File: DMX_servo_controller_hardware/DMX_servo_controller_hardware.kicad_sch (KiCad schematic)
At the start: 69 parts, among them J1 Power connector, J10 Conn_01x03, J11 Conn_01x03, J12 Conn_01x03, J15 To_XLR3, J3 Display, J4 Rotary encoder, J5 Conn_01x03, J6 Conn_01x03, J7 Conn_01x03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

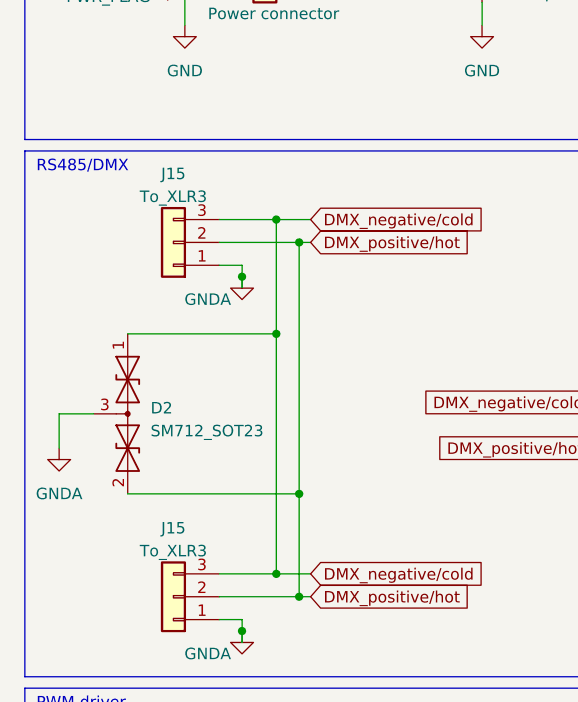
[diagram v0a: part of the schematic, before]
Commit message: Assigns footprint for test points
We might want to have all test points going to one connector (01x06 pin
header) to make the layout easier in the future.
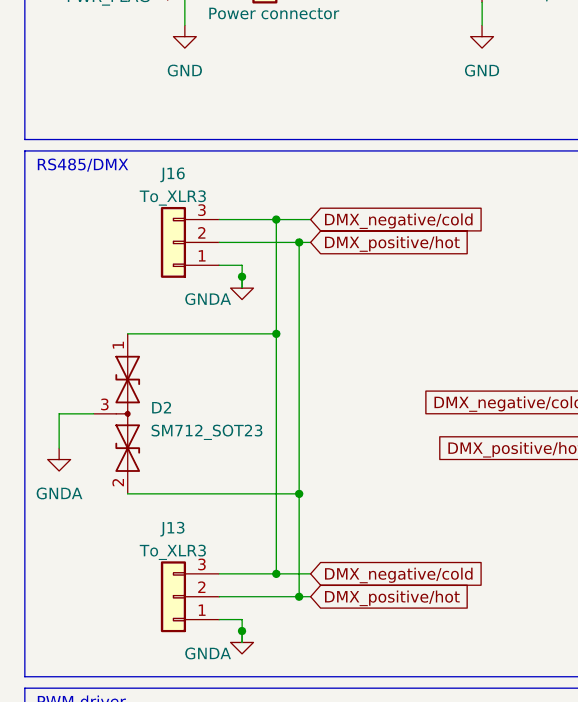
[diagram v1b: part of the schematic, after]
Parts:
- TP1, TP2, TP3, TP4, TP5, TP6, TP7, TP8: footprint (none) -> Connector_PinHeader_2.54mm:PinHeader_1x01_P2.54mm_Vertical
- renumbered J15 to J13, J15 to J16
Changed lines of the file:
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@@
       (effects (font (size 1.27 1.27)) (justify left))
     )
-    (property "Footprint" "" (at 124.46 149.86 0)
+    (property "Footprint" "Connector_PinHeader_2.54mm:PinHeader_1x01_P2.54mm_Vertical" (at 124.46 149.86 0)
       (effects (font (size 1.27 1.27)) hide)
     )
@@
       (effects (font (size 1.27 1.27)) (justify left))
     )
-    (property "Footprint" "" (at 124.46 157.48 0)
+    (property "Footprint" "Connector_PinHeader_2.54mm:PinHeader_1x01_P2.54mm_Vertical" (at 124.46 157.48 0)
       (effects (font (size 1.27 1.27)) hide)
     )
@@
       (effects (font (size 1.27 1.27)) (justify left))
     )
-    (property "Footprint" "" (at 124.46 160.02 0)
+    (property "Footprint" "Connector_PinHeader_2.54mm:PinHeader_1x01_P2.54mm_Vertical" (at 124.46 160.02 0)
       (effects (font (size 1.27 1.27)) hide)
     )
@@
       (effects (font (size 1.27 1.27)) (justify left))
     )
-    (property "Footprint" "" (at 124.46 152.4 0)
+    (property "Footprint" "Connector_PinHeader_2.54mm:PinHeader_1x01_P2.54mm_Vertical" (at 124.46 152.4 0)
       (effects (font (size 1.27 1.27)) hide)
     )
@@
       (effects (font (size 1.27 1.27)) (justify left))
     )
-    (property "Footprint" "" (at 124.46 162.56 0)
+    (property "Footprint" "Connector_PinHeader_2.54mm:PinHeader_1x01_P2.54mm_Vertical" (at 124.46 162.56 0)
       (effects (font (size 1.27 1.27)) hide)
     )
@@
       (effects (font (size 1.27 1.27)) (justify left))
     )
-    (property "Footprint" "" (at 124.46 154.94 0)
+    (property "Footprint" "Connector_PinHeader_2.54mm:PinHeader_1x01_P2.54mm_Vertical" (at 124.46 154.94 0)
       (effects (font (size 1.27 1.27)) hide)
     )
@@
   (symbol (lib_id "Connector_Generic:Conn_01x03") (at 29.21 97.79 180) (unit 1)
     (in_bom yes) (on_board yes) (dnp no) (fields_autoplaced)
-    (property "Reference" "J15" (at 29.21 90.17 0)
+    (property "Reference" "J13" (at 29.21 90.17 0)
       (effects (font (size 1.27 1.27)))
     )
@@
       (effects (font (size 1.27 1.27)) (justify left))
     )
-    (property "Footprint" "" (at 124.46 167.64 0)
+    (property "Footprint" "Connector_PinHeader_2.54mm:PinHeader_1x01_P2.54mm_Vertical" (at 124.46 167.64 0)
       (effects (font (size 1.27 1.27)) hide)
     )
@@
   (symbol (lib_id "Connector_Generic:Conn_01x03") (at 29.21 58.42 180) (unit 1)
     (in_bom yes) (on_board yes) (dnp no) (fields_autoplaced)
-    (property "Reference" "J15" (at 29.21 50.8 0)
+    (property "Reference" "J16" (at 29.21 50.8 0)
       (effects (font (size 1.27 1.27)))
     )
@@
       (effects (font (size 1.27 1.27)) (justify left))
     )
-    (property "Footprint" "" (at 124.46 165.1 0)
-      (effects (font (size 1.27 1.27)) hide)
-    )
+    (property "Footprint" "Connector_PinHeader_2.54mm:PinHeader_1x01_P2.54mm_Vertical" (at 124.46 165.1 0)
+      (effects (font (size 1.27 1.27)) hide)
+    )

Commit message: Reorder JST conectors and PCA9685 outputs for completion (OCD) / added DNP in 4out8 outputs / removed unnecessary resistor for upper 8 outputs of PCA9685 testpoints
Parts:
- removed R21, R22, R23, R24, R25, R26, R27, R28: 220Ω, Resistor_SMD:R_0815_2038Metric_Pad1.20x4.05mm_HandSolder, symbol Device:R_US
- J10, J11, J12, J9, R17, R18, R19, R20: now not fitted
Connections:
- net OUT1: now also J6.2 (Pin_2); no longer J7.2 (Pin_2)
- net OUT2: now also J7.2 (Pin_2); no longer J9.2 (Pin_2)
- net OUT3: now also J8.2 (Pin_2); no longer J11.2 (Pin_2)
- net OUT4: now also J9.2 (Pin_2); no longer J6.2 (Pin_2)
- net OUT5: now also J10.2 (Pin_2); no longer J8.2 (Pin_2)
- net OUT6: now also J11.2 (Pin_2); no longer J10.2 (Pin_2)
- net at U1.21 (LED14): now also TP7.1
- net at U1.20 (LED13): now also TP6.1
- net at U1.22 (LED15): now also TP8.1
- net at TP1.1: now also U1.15 (LED8)
- net at U1.16 (LED9): now also TP2.1
- net at U1.17 (LED10): now also TP3.1
- net at U1.18 (LED11): now also TP4.1
- net at U1.19 (LED12): now also TP5.1
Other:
- moved on the sheet: J6, J7, J8, R6, TP1, TP2, TP3, TP4, TP5, TP6, TP7, TP8

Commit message: Adds footprint for reset pushbutton
The footprint almost matches (and is definitely within tolerances) for
the technical drawing and measurements taken from the pushbuttons to be
used.
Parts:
- SW1: footprint (none) -> Button_Switch_SMD:SW_SPST_TL3342
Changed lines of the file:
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@@
       (effects (font (size 1.27 1.27)))
     )
-    (property "Footprint" "" (at 209.55 88.9 0)
+    (property "Footprint" "Button_Switch_SMD:SW_SPST_TL3342" (at 209.55 88.9 0)
       (effects (font (size 1.27 1.27)) hide)
     )

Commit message: Adds 6N137-X007T footprint and assigns it in schematics
The X007 variant of 6N137 uses an SMD gullwing package. The footprint
was created following the technical drawing in vishay's datasheet[1].

[1]: https://www.vishay.com/docs/84732/6n137.pdf
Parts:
- U3: footprint Package_DIP:DIP-8_W7.62mm -> DMX_servo_controller_hardware:6N137-X007T
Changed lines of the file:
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@@
       (effects (font (size 1.27 1.27)))
     )
-    (property "Footprint" "Package_DIP:DIP-8_W7.62mm" (at 151.13 81.28 0)
+    (property "Footprint" "DMX_servo_controller_hardware:6N137-X007T" (at 151.13 81.28 0)
       (effects (font (size 1.27 1.27)) hide)
     )

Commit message: Uses screw terminals for servo output connectors
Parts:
- J10, J11, J12, J5, J6, J7, J8, J9: footprint Connector_JST:JST_XH_B3B-XH-AM_1x03_P2.50mm_Vertical -> TerminalBlock:TerminalBlock_bornier-3_P5.08mm
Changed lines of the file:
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@@
       (effects (font (size 1.27 1.27)) (justify left))
     )
-    (property "Footprint" "Connector_JST:JST_XH_B3B-XH-AM_1x03_P2.50mm_Vertical" (at 182.88 123.19 0)
+    (property "Footprint" "TerminalBlock:TerminalBlock_bornier-3_P5.08mm" (at 182.88 123.19 0)
       (effects (font (size 1.27 1.27)) hide)
     )
@@
       (effects (font (size 1.27 1.27)) (justify left))
     )
-    (property "Footprint" "Connector_JST:JST_XH_B3B-XH-AM_1x03_P2.50mm_Vertical" (at 210.82 151.13 0)
+    (property "Footprint" "TerminalBlock:TerminalBlock_bornier-3_P5.08mm" (at 210.82 151.13 0)
       (effects (font (size 1.27 1.27)) hide)
     )
@@
       (effects (font (size 1.27 1.27)) (justify left))
     )
-    (property "Footprint" "Connector_JST:JST_XH_B3B-XH-AM_1x03_P2.50mm_Vertical" (at 210.82 123.19 0)
+    (property "Footprint" "TerminalBlock:TerminalBlock_bornier-3_P5.08mm" (at 210.82 123.19 0)
       (effects (font (size 1.27 1.27)) hide)
     )
@@
       (effects (font (size 1.27 1.27)) (justify left))
     )
-    (property "Footprint" "Connector_JST:JST_XH_B3B-XH-AM_1x03_P2.50mm_Vertical" (at 182.88 151.13 0)
+    (property "Footprint" "TerminalBlock:TerminalBlock_bornier-3_P5.08mm" (at 182.88 151.13 0)
       (effects (font (size 1.27 1.27)) hide)
     )
@@
       (effects (font (size 1.27 1.27)) (justify left))
     )
-    (property "Footprint" "Connector_JST:JST_XH_B3B-XH-AM_1x03_P2.50mm_Vertical" (at 238.76 151.13 0)
+    (property "Footprint" "TerminalBlock:TerminalBlock_bornier-3_P5.08mm" (at 238.76 151.13 0)
       (effects (font (size 1.27 1.27)) hide)
     )
@@
       (effects (font (size 1.27 1.27)) (justify left))
     )
-    (property "Footprint" "Connector_JST:JST_XH_B3B-XH-AM_1x03_P2.50mm_Vertical" (at 266.7 123.19 0)
+    (property "Footprint" "TerminalBlock:TerminalBlock_bornier-3_P5.08mm" (at 266.7 123.19 0)
       (effects (font (size 1.27 1.27)) hide)
     )
@@
       (effects (font (size 1.27 1.27)) (justify left))
     )
-    (property "Footprint" "Connector_JST:JST_XH_B3B-XH-AM_1x03_P2.50mm_Vertical" (at 238.76 123.19 0)
+    (property "Footprint" "TerminalBlock:TerminalBlock_bornier-3_P5.08mm" (at 238.76 123.19 0)
       (effects (font (size 1.27 1.27)) hide)
     )
@@
       (effects (font (size 1.27 1.27)) (justify left))
     )
-    (property "Footprint" "Connector_JST:JST_XH_B3B-XH-AM_1x03_P2.50mm_Vertical" (at 266.7 149.86 0)
-      (effects (font (size 1.27 1.27)) hide)
-    )
+    (property "Footprint" "TerminalBlock:TerminalBlock_bornier-3_P5.08mm" (at 266.7 149.86 0)
+      (effects (font (size 1.27 1.27)) hide)
+    )

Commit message: Uses DIP-8 footprint for SN65HVD12
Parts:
- U2: footprint Package_SO:SOIC-8_3.9x4.9mm_P1.27mm -> Package_DIP:DIP-8_W7.62mm
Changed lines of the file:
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@@
       (effects (font (size 1.27 1.27)) (justify right))
     )
-    (property "Footprint" "Package_SO:SOIC-8_3.9x4.9mm_P1.27mm" (at 110.49 55.88 0)
+    (property "Footprint" "Package_DIP:DIP-8_W7.62mm" (at 110.49 55.88 0)
       (effects (font (size 1.27 1.27)) hide)
     )

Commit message: Switches symbol and footprint for diode on VUSB
We're using the C211752[1] from yangjie, but since there's no schematic
symbol for it, I replaced it with the MRA4003T3G since it has the same
functionality and footprint and changed the value to reflect the correct
part number.

[1]: https://datasheet.lcsc.com/lcsc/1912111437_Yangzhou-Yangjie-Elec-Tech-M7_C211752.pdf
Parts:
- removed D1: 1N4001, Diode_THT:D_DO-41_SOD81_P10.16mm_Horizontal, symbol Diode:1N4001
- added D3: C211752 M7, Diode_SMD:D_SMA, symbol Diode:MRA4003T3G
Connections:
- net +5V: now also D3.2 (A)
- net at U4.40 (VBUS): now also D3.1 (K)
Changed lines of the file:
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@@
-    )
-  )
-  (symbol (lib_id "Diode:1N4001") (at 259.08 27.94 90) (unit 1)
-    (in_bom yes) (on_board yes) (dnp no) (fields_autoplaced)
-    (property "Reference" "D1" (at 261.62 27.305 90)
-      (effects (font (size 1.27 1.27)) (justify right))
-    )
-    (property "Value" "1N4001" (at 261.62 29.845 90)
-      (effects (font (size 1.27 1.27)) (justify right))
-    )
-    (property "Footprint" "Diode_THT:D_DO-41_SOD81_P10.16mm_Horizontal" (at 259.08 27.94 0)
-      (effects (font (size 1.27 1.27)) hide)
-    )
-    (property "Datasheet" "http://www.vishay.com/docs/88503/1n4001.pdf" (at 259.08 27.94 0)
-      (effects (font (size 1.27 1.27)) hide)
-    )
-    (pin "1")
-    (pin "2")
-    (instances
-      (project "DMX_servo_controller_hardware"
-        (path "/cd90393c-7fb4-4867-84b8-7df1a2bf6613"
-          (reference "D1") (unit 1)
-        )
-      )
     )
   )
@@
         )
       )
+    )
+  )
+  (symbol (lib_id "Diode:MRA4003T3G") (at 259.08 27.94 90) (unit 1)
+    (in_bom yes) (on_board yes) (dnp no) (fields_autoplaced)
+    (property "Reference" "D3" (at 261.62 27.305 90)
+      (effects (font (size 1.27 1.27)) (justify right))
+    )
+    (property "Value" "C211752 M7" (at 261.62 29.845 90)
+      (effects (font (size 1.27 1.27)) (justify right))
+    )
+    (property "Footprint" "Diode_SMD:D_SMA" (at 263.525 27.94 0)
+      (effects (font (size 1.27 1.27)) hide)
+    )
+    (property "Datasheet" "https://datasheet.lcsc.com/lcsc/1912111437_Yangzhou-Yangjie-Elec-Tech-M7_C211752.pdf" (at 259.08 27.94 0)
+      (effects (font (size 1.27 1.27)) hide)
+    )
+    (pin "1")
+    (pin "2")
+    (instances
+      (project "DMX_servo_controller_hardware"
+        (path "/cd90393c-7fb4-4867-84b8-7df1a2bf6613"
+          (reference "D3") (unit 1)
+        )
+      )

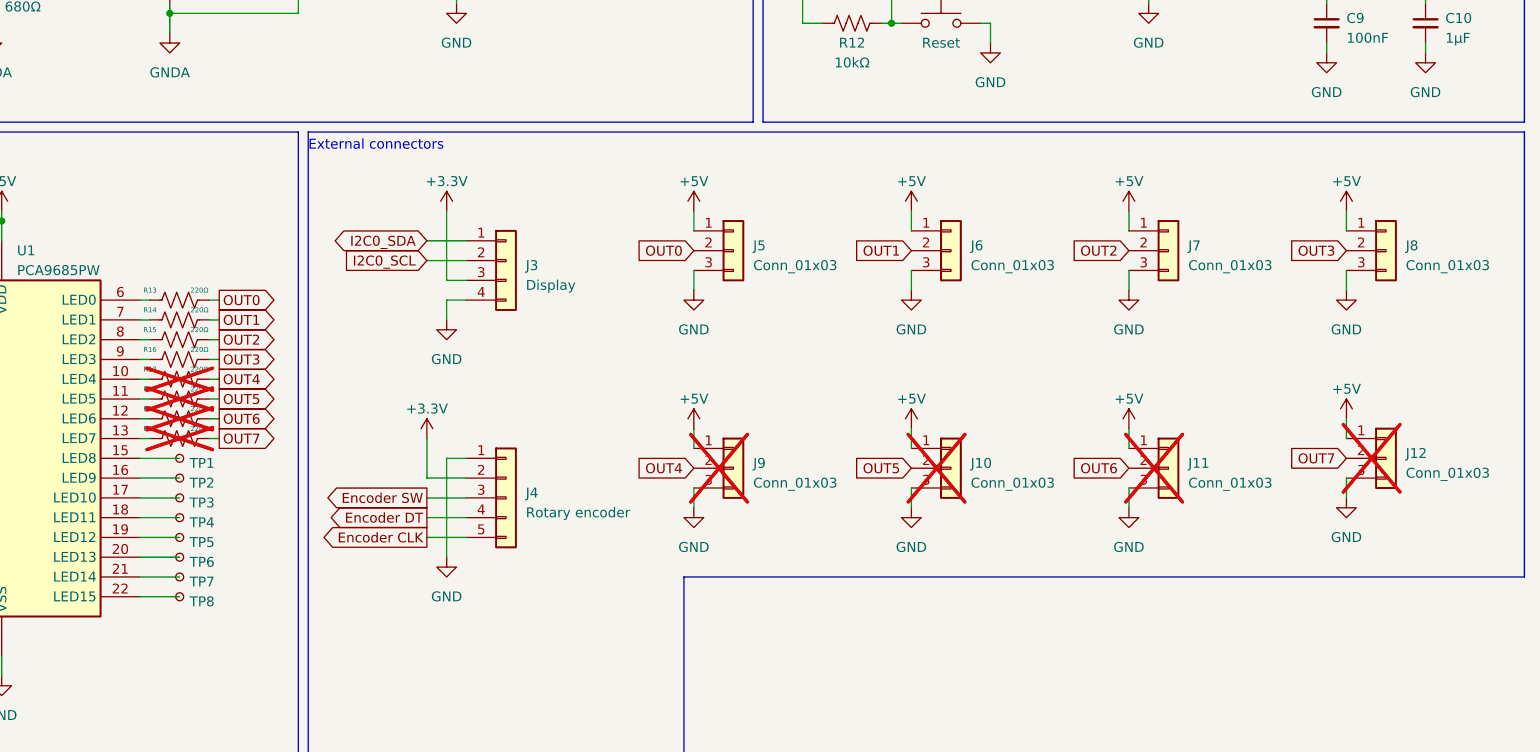
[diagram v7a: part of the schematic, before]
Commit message: Adds output for all PWM channels
They are marked as unpopulated, but it's a good idea to route all
outputs since we can than populate them if we want more channels.
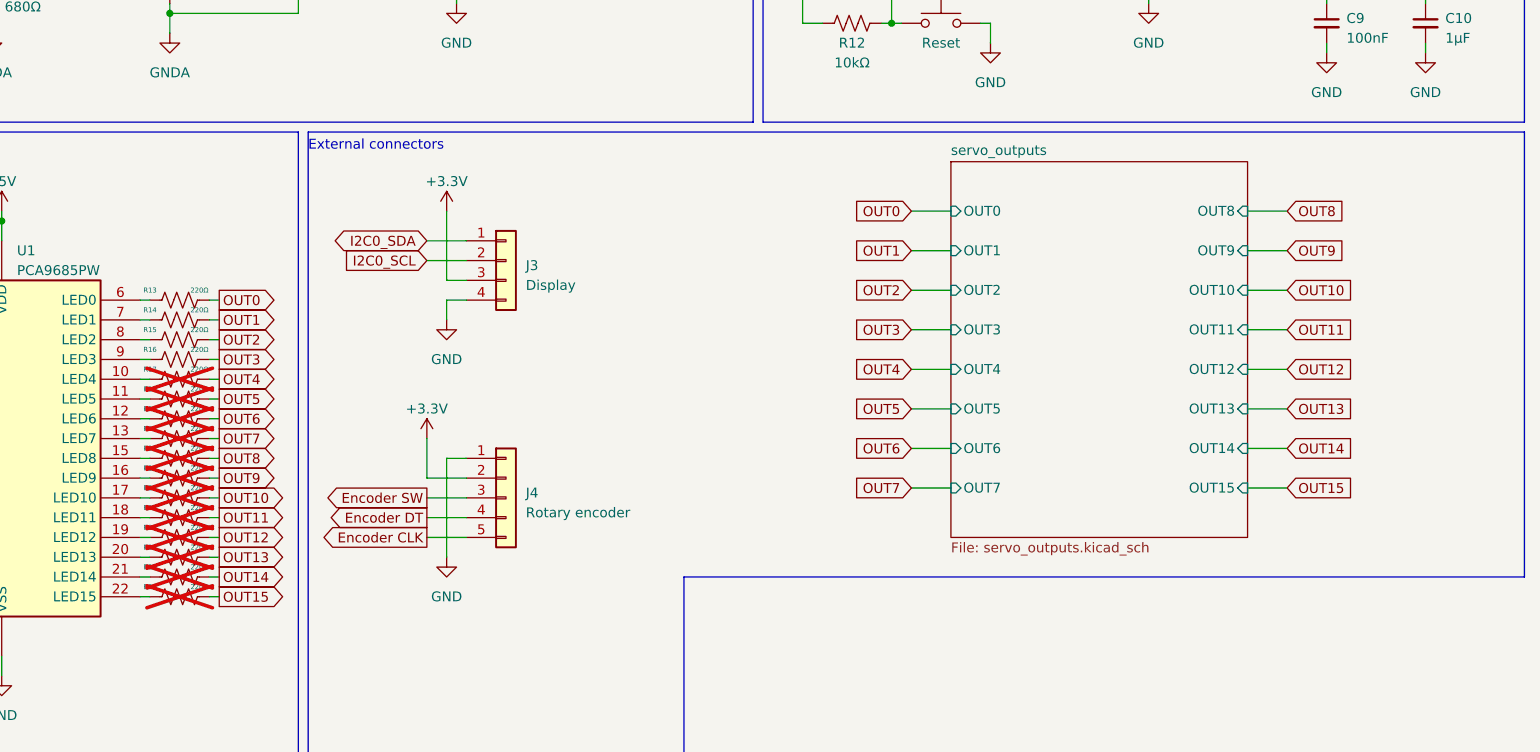
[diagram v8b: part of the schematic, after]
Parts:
- removed J10, J11, J12, J5, J6, J7, J8, J9: Conn_01x03, TerminalBlock:TerminalBlock_bornier-3_P5.08mm, symbol Connector_Generic:Conn_01x03
- removed TP1, TP2, TP3, TP4, TP5, TP6, TP7, TP8: ~, Connector_PinHeader_2.54mm:PinHeader_1x01_P2.54mm_Vertical, symbol Connector:TestPoint_Small
- added R21, R22, R23, R24, R25, R26, R27, R28: 220Ω, Resistor_SMD:R_0815_2038Metric_Pad1.20x4.05mm_HandSolder, symbol Device:R_US
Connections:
- net at U1.15 (LED8): now also R21.1
- net at U1.16 (LED9): now also R22.1
- net at U1.17 (LED10): now also R23.1
- net at U1.18 (LED11): now also R24.1
- net at U1.19 (LED12): now also R25.1
- net at U1.20 (LED13): now also R26.1
- net at U1.21 (LED14): now also R27.1
- net at U1.22 (LED15): now also R28.1
- new net OUT10: R23.2
- new net OUT11: R24.2
- new net OUT12: R25.2
- new net OUT13: R26.2
- new net OUT14: R27.2
- new net OUT15: R28.2
- new net OUT8: R21.2
- new net OUT9: R22.2
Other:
- added sheet servo_outputs (servo_outputs.kicad_sch)
